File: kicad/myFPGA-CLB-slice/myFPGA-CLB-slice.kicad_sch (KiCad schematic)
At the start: 35 parts, among them J1 Conn_01x04, J10 Conn_01x02, J11 Conn_01x04, J12 Conn_01x04, J2 Conn_01x04, J3 Conn_01x04, J4 Conn_01x04, J5 Conn_01x04, J6 Conn_01x04, J7 Conn_01x04, J8 Conn_01x04, J9 Conn_01x02, U16 NC7SB3157P6X, U37 74AHCT595, U38 NC7SB3157P6X

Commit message: fixed kicad names, updated architecure, started CBv
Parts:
- removed C4: 100n, Capacitor_SMD:C_0805_2012Metric, symbol Device:C
- removed J12: Conn_01x04, symbol Connector_Generic:Conn_01x04
- removed R8: 10k, symbol Device:R
- added C2: 22u, Resistor_SMD:R_1206_3216Metric, symbol Device:C_Polarized
- added C?: 100n, Capacitor_SMD:C_0805_2012Metric, symbol Device:C
- added J13, J14, J6: Conn_01x04, symbol Connector_Generic:Conn_01x04
- added R? (x3): 100k, Resistor_SMD:R_0805_2012Metric, symbol Device:R
- C4: renamed from C36; value 100u -> 22u; footprint (none) -> Resistor_SMD:R_1206_3216Metric; Dielectric (none) -> X5R; JLCPCB Part # (none) -> C5672; Part Nr. (none) -> CL31A226KPHNNNE; Voltage (none) -> 10V
- C?: renamed from C5; Dielectric (none) -> X7R; JLCPCB Part # (none) -> C49678; Part Nr. (none) -> CC0805KRX7R9BB104; Voltage (none) -> 50V
- D?: renamed from D5; value LED -> LED (green); footprint (none) -> LED_SMD:LED_0805_2012Metric; JLCPCB Part # (none) -> C2297; Part Nr. (none) -> C2297
- D?: renamed from D7; value LED -> LED (green); footprint (none) -> LED_SMD:LED_0805_2012Metric; JLCPCB Part # (none) -> C2297; Part Nr. (none) -> C2297
- D?: renamed from D3; value LED -> LED (green); footprint (none) -> LED_SMD:LED_0805_2012Metric; JLCPCB Part # (none) -> C2297; Part Nr. (none) -> C2297
- D?: renamed from D6; value LED -> LED (green); footprint (none) -> LED_SMD:LED_0805_2012Metric; JLCPCB Part # (none) -> C2297; Part Nr. (none) -> C2297
- D?: renamed from D4; value LED -> LED (green); footprint (none) -> LED_SMD:LED_0805_2012Metric; JLCPCB Part # (none) -> C2297; Part Nr. (none) -> C2297
- D?: renamed from D1; value LED -> LED (green); footprint (none) -> LED_SMD:LED_0805_2012Metric; JLCPCB Part # (none) -> C2297; Part Nr. (none) -> C2297
- D?: renamed from D2; value LED -> LED (green); footprint (none) -> LED_SMD:LED_0805_2012Metric; JLCPCB Part # (none) -> C2297; Part Nr. (none) -> C2297
- D?: renamed from D8; value LED -> LED (green); footprint (none) -> LED_SMD:LED_0805_2012Metric; JLCPCB Part # (none) -> C2297; Part Nr. (none) -> C2297
- J1: renamed from J7; JLCPCB Part # (none) -> do not place; Part Nr. (none) -> do not place
- J10: renamed from J5; JLCPCB Part # (none) -> do not place; Part Nr. (none) -> do not place
- J11: renamed from J6; JLCPCB Part # (none) -> do not place; Part Nr. (none) -> do not place
- J12: renamed from J1; JLCPCB Part # (none) -> do not place; Part Nr. (none) -> do not place
- J2: renamed from J8; JLCPCB Part # (none) -> do not place; Part Nr. (none) -> do not place
- J3: renamed from J2; JLCPCB Part # (none) -> do not place; Part Nr. (none) -> do not place
- J4: renamed from J3; JLCPCB Part # (none) -> do not place; Part Nr. (none) -> do not place
- J5: renamed from J4; JLCPCB Part # (none) -> do not place; Part Nr. (none) -> do not place
- J7: renamed from J11; JLCPCB Part # (none) -> do not place; Part Nr. (none) -> do not place
- J8: renamed from J9; JLCPCB Part # (none) -> do not place; Part Nr. (none) -> do not place
- J9: renamed from J10; JLCPCB Part # (none) -> do not place; Part Nr. (none) -> do not place
- R?: renamed from R3; footprint (none) -> Resistor_SMD:R_0805_2012Metric; JLCPCB Part # (none) -> C17630; Part Nr. (none) -> 0805W8F3300T5E
- R?: renamed from R5; footprint (none) -> Resistor_SMD:R_0805_2012Metric; JLCPCB Part # (none) -> C17630; Part Nr. (none) -> 0805W8F3300T5E
- R?: renamed from R4; footprint (none) -> Resistor_SMD:R_0805_2012Metric; JLCPCB Part # (none) -> C17630; Part Nr. (none) -> 0805W8F3300T5E
- R?: renamed from R8; footprint (none) -> Resistor_SMD:R_0805_2012Metric; JLCPCB Part # (none) -> C17630; Part Nr. (none) -> 0805W8F3300T5E
- R?: renamed from R6; footprint (none) -> Resistor_SMD:R_0805_2012Metric; JLCPCB Part # (none) -> C17630; Part Nr. (none) -> 0805W8F3300T5E
- R?: renamed from R2; footprint (none) -> Resistor_SMD:R_0805_2012Metric; JLCPCB Part # (none) -> C17630; Part Nr. (none) -> 0805W8F3300T5E
- R?: renamed from R7; footprint (none) -> Resistor_SMD:R_0805_2012Metric; JLCPCB Part # (none) -> C17630; Part Nr. (none) -> 0805W8F3300T5E
- R?: renamed from R1; footprint (none) -> Resistor_SMD:R_0805_2012Metric; JLCPCB Part # (none) -> C17630; Part Nr. (none) -> 0805W8F3300T5E
- renumbered U16 to U1, U38 to U1, U37 to U2
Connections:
- net +3V3: now also J6.1 (Pin_1); no longer J7.2 (Pin_2), U2.16 (VCC)
- net GND: now also J7.2 (Pin_2), C2.2, C?.2, J6.2 (Pin_2), J6.3 (Pin_3), R?.2, R?.2, R?.2; no longer J7.4 (Pin_4)
- net Input Selector/CBN_0: now also J3.1 (Pin_1); no longer J3.4 (Pin_4)
- net Input Selector/CBN_1: now also J3.2 (Pin_2); no longer J3.3 (Pin_3)
- net Input Selector/CBN_2: now also J3.3 (Pin_3); no longer J3.2 (Pin_2)
- net Input Selector/CBN_3: now also J3.4 (Pin_4); no longer J3.1 (Pin_1)
- net Input Selector/CBS_0: now also J4.1 (Pin_1); no longer J4.4 (Pin_4)
- net Input Selector/CBS_1: now also J4.2 (Pin_2); no longer J4.3 (Pin_3)
- net Input Selector/CBS_2: now also J4.3 (Pin_3); no longer J4.2 (Pin_2)
- net Input Selector/CBS_3: now also J4.4 (Pin_4); no longer J4.1 (Pin_1)
- net REG: no longer J10.3 (Pin_3), J11.3 (Pin_3)
- net set_clk_sel: now also R?.1
- net CBw_2: now reaches J1.3 (Pin_3)
- net CBw_3: now reaches J1.4 (Pin_4)
- net D-Latch/Oa renamed D-Latch/Qa
- net D-Latch/Ob renamed D-Latch/Qb
- net D-Latch/Oc renamed D-Latch/Qc
- net D-Latch/Od renamed D-Latch/Qd
- net Input Selector/CBW_0 renamed CBw_0
- net Input Selector/CBW_1 renamed CBw_1
- net Input Selector/presel_0 renamed CBpre_3
- net CBpre_3: now also R?.1
- net Input Selector/presel_1 renamed CBpre_2
- net CBpre_2: now also R?.1
- net LUT4_0/I2 renamed CBpre_1
- net LUT4_0/I3 renamed CBpre_0
- new net: J13.1 (Pin_1), J14.1 (Pin_1)
- new net: J13.2 (Pin_2), J14.2 (Pin_2)
- new net: J13.3 (Pin_3), J14.3 (Pin_3)
- new net: J13.4 (Pin_4), J14.4 (Pin_4)
- new net +3.3VP: C2.1, C?.1, J6.4 (Pin_4), J7.4 (Pin_4), U2.16 (VCC)
- new net LACTH: J11.3 (Pin_3)
- new net LATCH: J10.3 (Pin_3)
- no-connect marks 2 -> 0
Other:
- sheet D-Latch ports: added Qa, Qb, Qc, Qd; removed Ua, Ub, Uc, Ud
- sheet Input Selector ports: added CBW_2, CBW_3; removed none
- note added: "SPI return path"
- note added: "SPI through path"
- moved on the sheet: C4, C?, J1, J10, J11, J3, J4, J5, J7

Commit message: kicad -> pcb started
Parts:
- removed J13, J14: Conn_01x04, symbol Connector_Generic:Conn_01x04
- added J15: Conn_01x04, Connector_PinHeader_2.54mm:PinHeader_1x04_P2.54mm_Vertical, symbol Connector_Generic:Conn_01x04
- C2, C4: Dielectric X5R -> (none); JLCPCB Part # C5672 -> (none); Part Nr. CL31A226KPHNNNE -> (none); Voltage 10V -> (none)
- C? (x2): footprint Capacitor_SMD:C_0805_2012Metric -> Capacitor_SMD:C_0603_1608Metric; Dielectric X7R -> (none); JLCPCB Part # C49678 -> (none); Part Nr. CC0805KRX7R9BB104 -> (none); Voltage 50V -> (none)
- J1, J2, J3, J4, J5, J6, J7: footprint (none) -> Connector_PinHeader_2.54mm:PinHeader_1x04_P2.54mm_Vertical
- J12: renamed from J10; footprint (none) -> Connector_PinHeader_2.54mm:PinHeader_1x04_P2.54mm_Vertical
- J13: renamed from J12; footprint (none) -> Connector_PinHeader_2.54mm:PinHeader_1x04_P2.54mm_Vertical
- J14: renamed from J11; footprint (none) -> Connector_PinHeader_2.54mm:PinHeader_1x04_P2.54mm_Vertical
- J8, J9: footprint (none) -> Connector_PinHeader_2.54mm:PinHeader_1x02_P2.54mm_Vertical
- R? (x8): footprint Resistor_SMD:R_0805_2012Metric -> Resistor_SMD:R_0603_1608Metric; JLCPCB Part # C17630 -> (none); Part Nr. 0805W8F3300T5E -> (none)
- R? (x3): footprint Resistor_SMD:R_0805_2012Metric -> Resistor_SMD:R_0603_1608Metric; JLCPCB Part # C149504 -> (none); Part Nr. 0805W8F1003T5E -> (none)
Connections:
- net GND: now also J15.1 (Pin_1), J15.3 (Pin_3)
- net clk_0: now reaches J2.2 (Pin_2), U1.3
- net clk_0: now also J15.2 (Pin_2)
- net clk_1: now reaches J2.4 (Pin_4), U1.1
- net clk_1: now also J15.4 (Pin_4)
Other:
- note added: "clk out"
- note removed: "SPI return path"
- moved on the sheet: R?, U1A

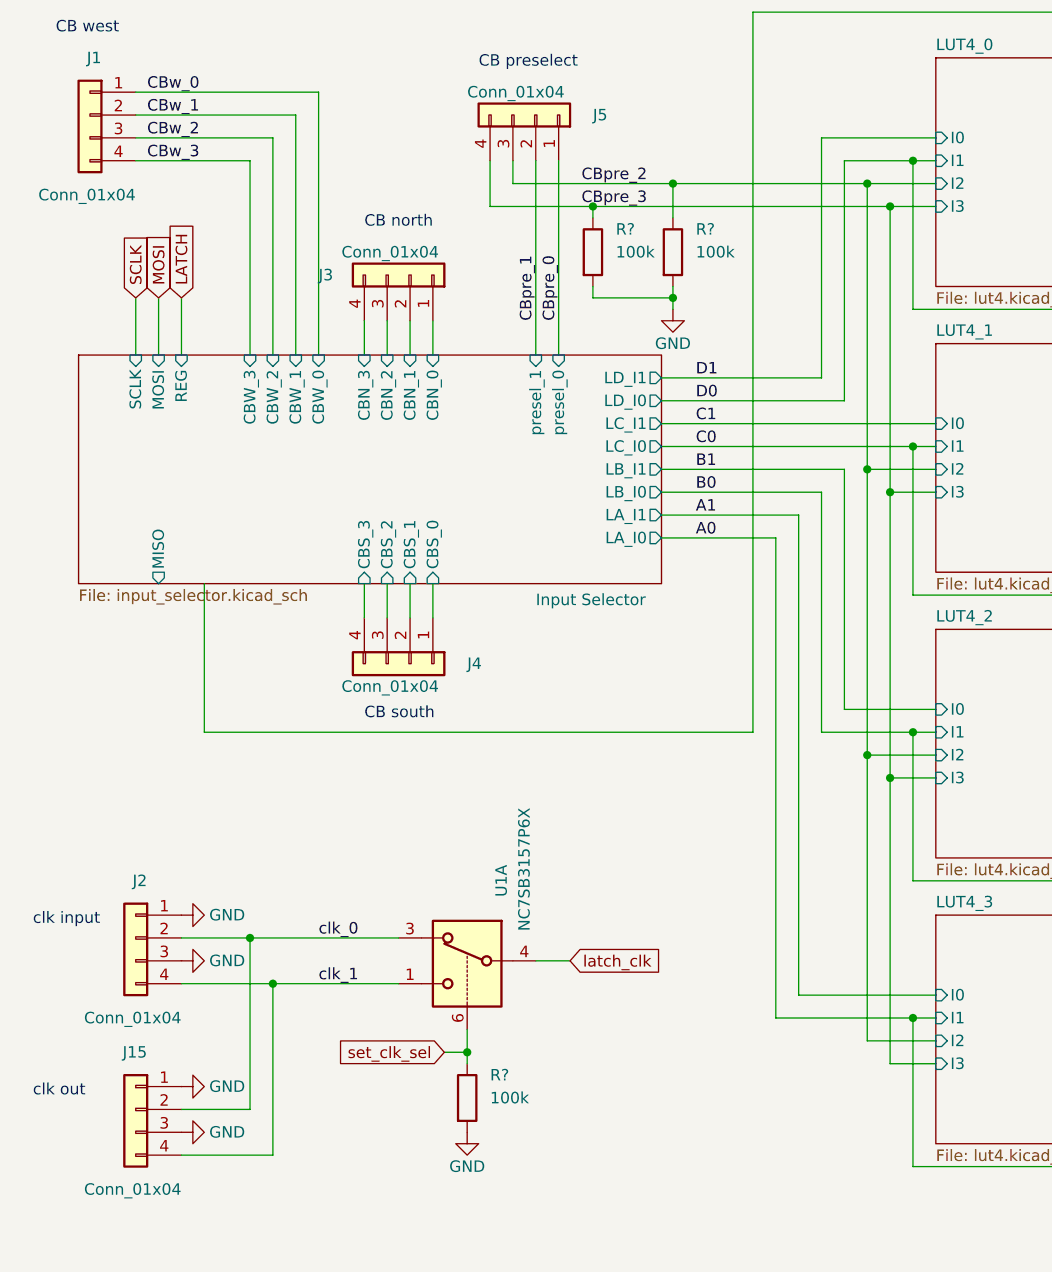
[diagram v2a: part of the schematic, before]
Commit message: kicad: picked JLC parts, fixed routing to match VHDL, started layouting
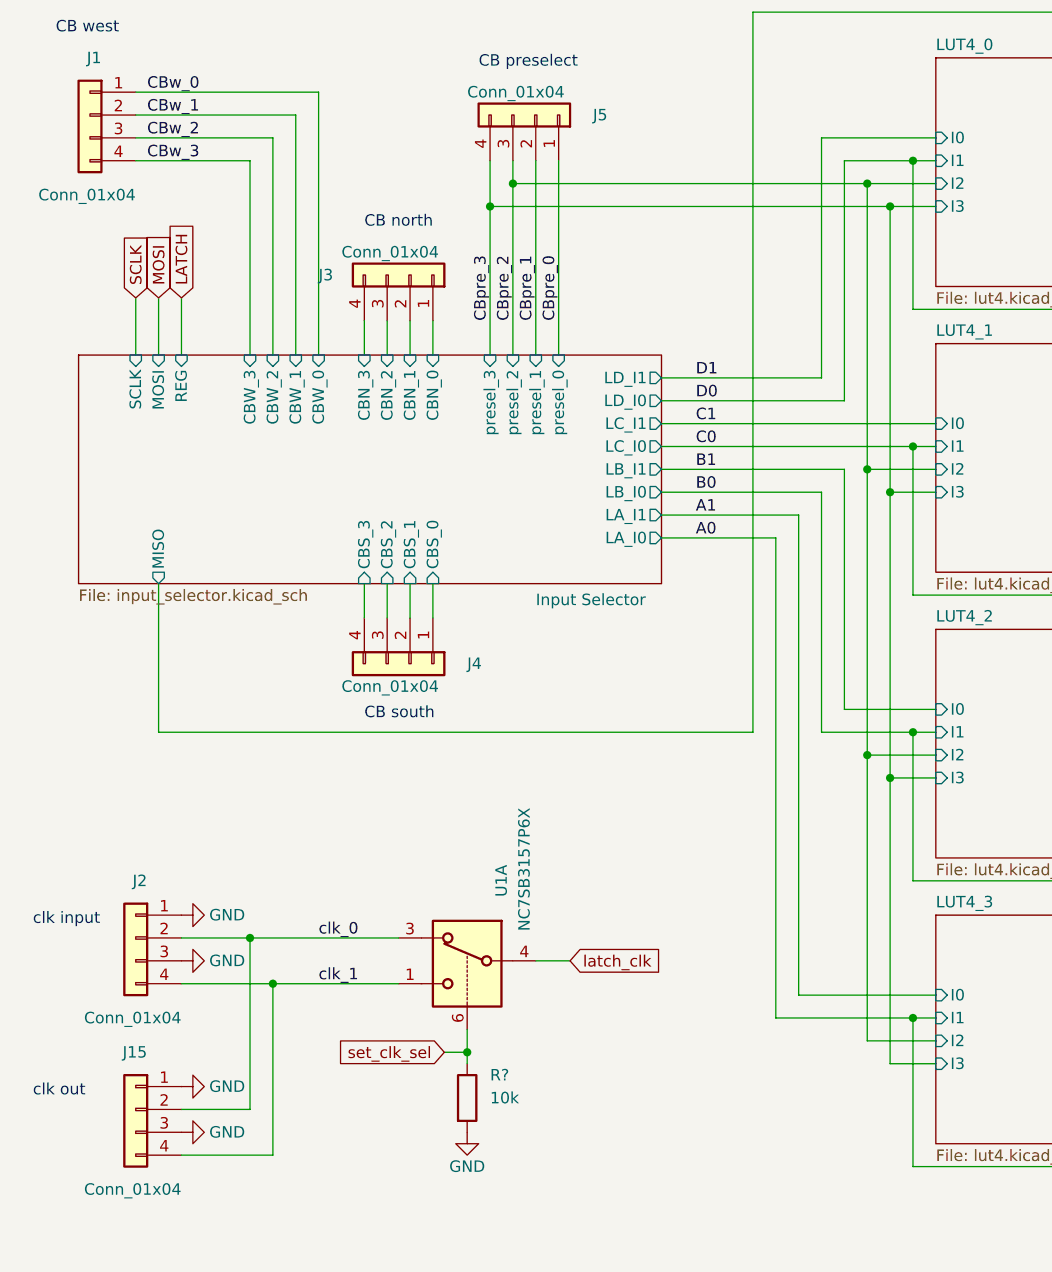
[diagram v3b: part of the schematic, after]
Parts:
- removed R? (x2): 100k, Resistor_SMD:R_0603_1608Metric, symbol Device:R
- C2, C4: Dielectric (none) -> X5R; JLCPCB Part # (none) -> C12891; Part Nr. (none) -> CL31A226KAHNNNE; Voltage (none) -> 25
- C? (x2): Dielectric (none) -> X7R; JLCPCB Part # (none) -> C14663; Part Nr. (none) -> CC0603KRX7R9BB104; Voltage (none) -> 50
- J1, J12, J13, J14, J15, J2, J3, J4, J5, J6, J7, J8, J9: JLCPCB Alt # (none) -> do not place
- R? (x8): JLCPCB Part # (none) -> C23138; Part Nr. (none) -> 0603WAF3300T5E
- R?: value 100k -> 10k; JLCPCB Part # (none) -> C25804; Part Nr. (none) -> 0603WAF1002T5E
- U2: JLCPCB Alt # (none) -> C431479 / 74HC595D / SOIC-16-3.9; package (none) -> SOIC-16-3.9
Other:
- sheet Input Selector ports: added presel_2, presel_3; removed none

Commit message: restart PCB layout
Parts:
- J1, J12, J13, J14, J15, J2, J3, J4, J5, J6, J7: footprint Connector_PinHeader_2.54mm:PinHeader_1x04_P2.54mm_Vertical -> Connector_PinHeader_2.54mm:PinHeader_1x04_P2.54mm_Horizontal
- J8, J9: footprint Connector_PinHeader_2.54mm:PinHeader_1x02_P2.54mm_Vertical -> Connector_PinHeader_2.54mm:PinHeader_1x02_P2.54mm_Horizontal
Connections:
- net LACTH is gone; now on net MISO: J14.3 (Pin_3)
- net REG is gone; now on net LATCH: U2.12 (RCLK)
- net +3.3VP: now also J7.1 (Pin_1); no longer J7.4 (Pin_4)
- net +3V3: now also J7.4 (Pin_4); no longer J7.1 (Pin_1)
- net GND: now also J14.1 (Pin_1), J15.2 (Pin_2), J15.4 (Pin_4); no longer J14.4 (Pin_4), J15.1 (Pin_1), J15.3 (Pin_3)
- net LATCH: now also J14.2 (Pin_2)
- net MISO: no longer J14.2 (Pin_2)
- net SCLK: now also J14.4 (Pin_4); no longer J14.1 (Pin_1)
- net clk_0: now also J15.3 (Pin_3); no longer J15.2 (Pin_2)
- net clk_1: now also J15.1 (Pin_1); no longer J15.4 (Pin_4)
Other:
- sheet LUT4_0 ports: added LATCH; removed REG
- sheet LUT4_1 ports: added LATCH; removed REG
- sheet LUT4_2 ports: added LATCH; removed REG
- sheet LUT4_3 ports: added LATCH; removed REG
- moved on the sheet: J15, J7

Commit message: progress in pcb of CLB
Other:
- sheet D-Latch ports: added aresetn; removed none
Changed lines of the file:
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@@
     (stroke (width 0) (type default))
   )
+  (wire (pts (xy 228.6 62.23) (xy 231.14 62.23))
+    (stroke (width 0) (type default))
+  )
   (wire (pts (xy 248.92 137.16) (xy 252.73 137.16))
     (stroke (width 0) (type default))
@@
     )
   )
+  (global_label "aresetn" (shape input) (at 228.6 62.23 180) (fields_autoplaced)
+    (effects (font (size 1.27 1.27)) (justify right))
+    (property "Intersheetrefs" "${INTERSHEET_REFS}" (at 218.5996 62.23 0)
+      (effects (font (size 1.27 1.27)) (justify right) hide)
+    )
+  )
   (global_label "MISO" (shape input) (at 267.97 152.4 180) (fields_autoplaced)
     (effects (font (size 1.27 1.27)) (justify right))
@@
     )
   )
+  (global_label "aresetn" (shape input) (at 209.55 152.4 180) (fields_autoplaced)
+    (effects (font (size 1.27 1.27)) (justify right))
+    (property "Intersheetrefs" "${INTERSHEET_REFS}" (at 199.5496 152.4 0)
+      (effects (font (size 1.27 1.27)) (justify right) hide)
+    )
+  )
   (global_label "MOSI" (shape input) (at 245.11 152.4 0) (fields_autoplaced)
     (effects (font (size 1.27 1.27)) (justify left))
@@
       (effects (font (size 1.27 1.27)) (justify left))
     )
+    (pin "aresetn" input (at 231.14 62.23 180)
+      (effects (font (size 1.27 1.27)) (justify left))
+    )

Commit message: progress in pcb of CLB
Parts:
- removed D? (x2): LED (green), LED_SMD:LED_0805_2012Metric, symbol Device:LED
- removed R? (x2): 330R, Resistor_SMD:R_0603_1608Metric, symbol Device:R
- added C? (x3): 100n, Capacitor_SMD:C_0603_1608Metric, symbol Device:C
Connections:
- net +3.3VP: now also C?.1
- net +3V3: now also C?.1, C?.1
- net GND: now also C?.2, C?.2, C?.2
- no-connect marks 0 -> 2
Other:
- sheet Input Selector ports: added LATCH; removed REG

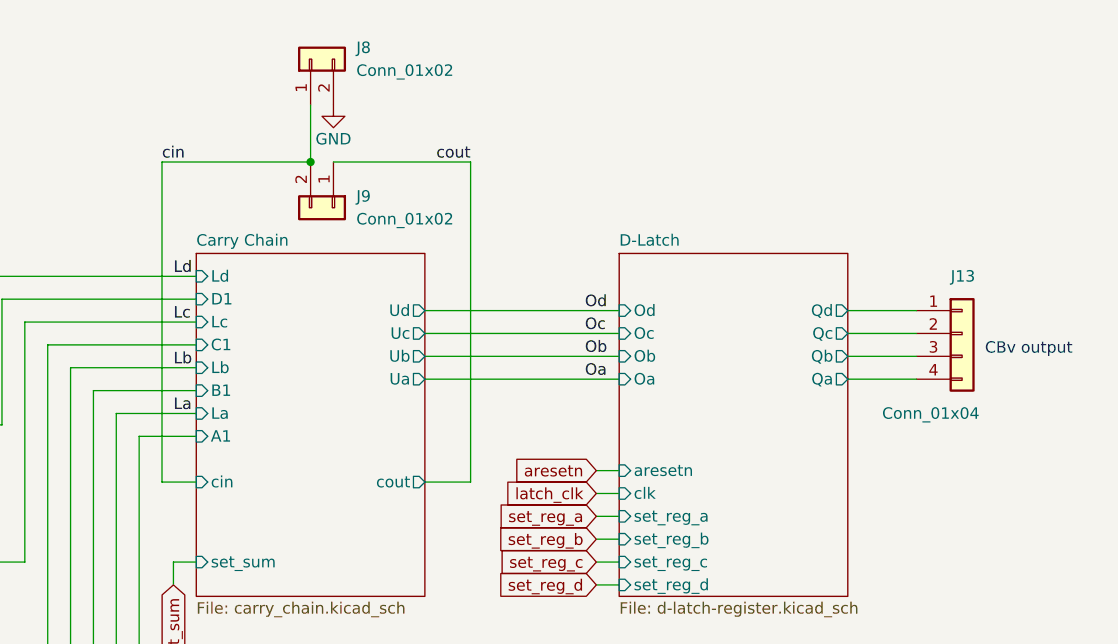
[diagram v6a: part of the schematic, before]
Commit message: 2 layer pcb for clb seems complete (awaits review)
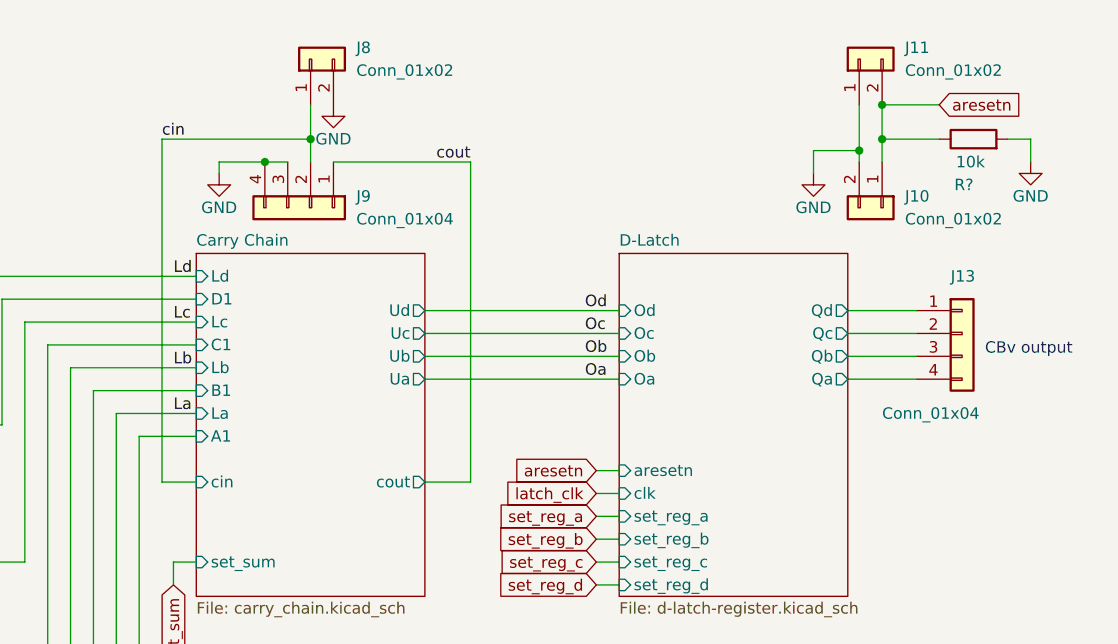
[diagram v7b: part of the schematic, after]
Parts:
- removed J9: Conn_01x02, Connector_PinHeader_2.54mm:PinHeader_1x02_P2.54mm_Horizontal, symbol Connector_Generic:Conn_01x02
- added J10, J11: Conn_01x02, Connector_PinHeader_2.54mm:PinHeader_1x02_P2.54mm_Horizontal, symbol Connector_Generic:Conn_01x02
- added J9: Conn_01x04, Connector_PinHeader_2.54mm:PinHeader_1x04_P2.54mm_Horizontal, symbol Connector_Generic:Conn_01x04
- added R?: 10k, Resistor_SMD:R_0603_1608Metric, symbol Device:R
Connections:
- net GND: now also J10.2 (Pin_2), J11.1 (Pin_1), J9.3 (Pin_3), J9.4 (Pin_4), R?.2
- net aresetn: now also J10.1 (Pin_1), J11.2 (Pin_2), R?.1
- net cin: now also J9.2 (Pin_2)
- net cout: now also J9.1 (Pin_1)
